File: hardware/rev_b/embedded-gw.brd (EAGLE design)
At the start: 38.5 x 55.5 mm, 57 parts, among them J1 DM3BT-DSF-PEJS, J2 TC2030-JLINK-NL, J3 USB-A-MALE-PLUG, Q1 DMN32D2LDF, U1 AP7362A-33SP-13, U2 BT840X, U3 CP2102N-20, U4 ESDR0502N, U5 ESP32-WROVER-E, U6 ESP32-WROVER-E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

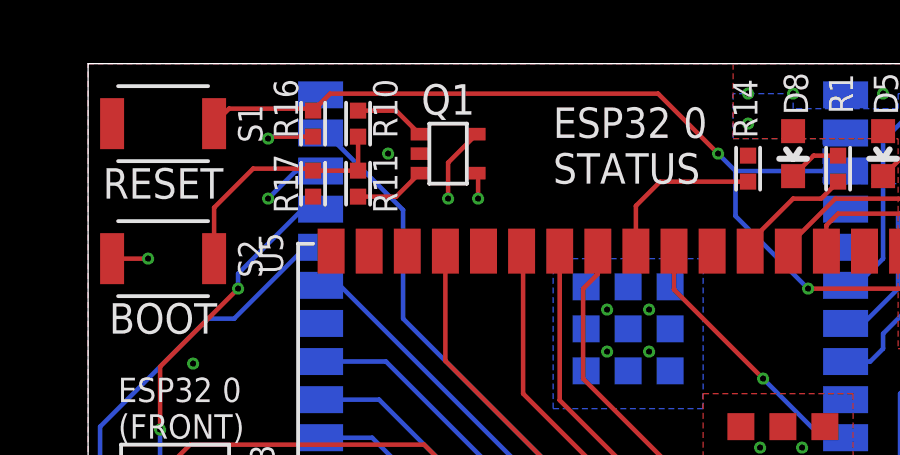
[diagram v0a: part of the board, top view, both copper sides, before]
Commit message: Swap Q1 with QS5K2TR
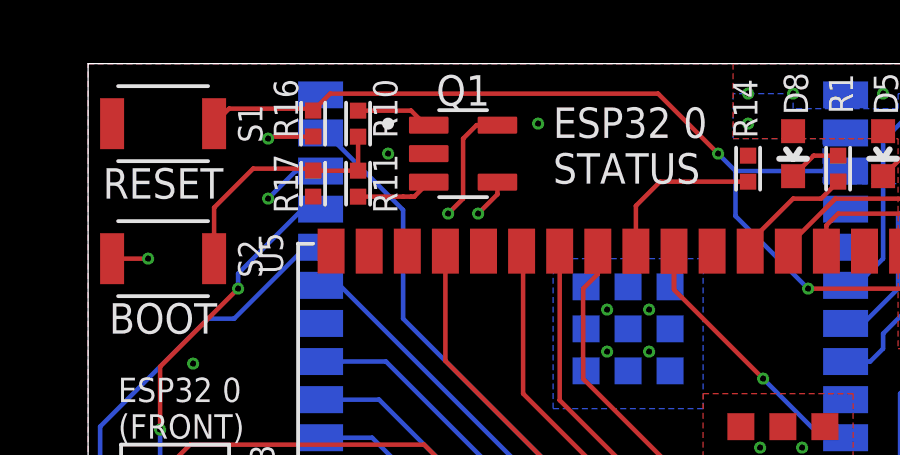
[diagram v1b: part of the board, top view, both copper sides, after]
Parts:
- Q1: value DMN32D2LDF -> QS5K2TR; device fets:SOT353 -> fets:SOT95P280X100-5N
- moved Q1 0.50 mm to (12.5, 52.5), turned to 0 degrees
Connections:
- net GND: now also Q1.2; no longer Q1.S
- net IO0: now also Q1.5; no longer Q1.D1
- net N$1: now also Q1.1; no longer Q1.G1
- net N$4: now also Q1.3; no longer Q1.G2
- net SD_HOST_D0: now also Q1.4; no longer Q1.D2
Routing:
- net IO0: track 27.6 -> 28.6 mm
- net GND: vias 43 -> 44
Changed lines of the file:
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@@
 <layer number="25" name="tNames" color="7" fill="1" visible="yes" active="yes"/>
 <layer number="26" name="bNames" color="7" fill="1" visible="yes" active="yes"/>
-<layer number="27" name="tValues" color="7" fill="1" visible="yes" active="yes"/>
+<layer number="27" name="tValues" color="7" fill="1" visible="no" active="yes"/>
 <layer number="28" name="bValues" color="7" fill="1" visible="no" active="yes"/>
 <layer number="29" name="tStop" color="7" fill="3" visible="no" active="yes"/>
@@
 <attribute name="VALUE" x="7.603" y="51.5" size="1.016" layer="27" font="vector" ratio="12" rot="R270" align="bottom-center"/>
 </element>
-<element name="Q1" library="fets" package="SOT353" value="DMN32D2LDF" x="12" y="52.5" smashed="yes" rot="R90">
-<attribute name="DIGIKEY" value="DMN32D2LDF-7DICT-ND" x="12" y="52.5" size="1.778" layer="27" rot="R90" display="off"/>
-<attribute name="MANUFACTURER" value="Diodes Incorporated" x="12" y="52.5" size="1.778" layer="27" rot="R90" display="off"/>
-<attribute name="MPN" value="DMN32D2LDF-7" x="12" y="52.5" size="1.778" layer="27" rot="R90" display="off"/>
-<attribute name="NAME" x="12" y="53.8" size="1.016" layer="25" font="vector" ratio="12" align="bottom-center"/>
-<attribute name="VALUE" x="12" y="54.2905" size="1.016" layer="27" font="vector" ratio="12" rot="R180" align="top-center"/>
+<element name="Q1" library="fets" package="SOT95P280X100-5N" value="QS5K2TR" x="12.5" y="52.5" smashed="yes">
+<attribute name="NAME" x="12.5" y="54.1" size="1.016" layer="25" font="vector" ratio="12" align="bottom-center"/>
+<attribute name="VALUE" x="14.2905" y="52.5" size="1.016" layer="27" font="vector" ratio="12" rot="R90" align="top-center"/>
 </element>
 <element name="D2" library="passives" package="0201_DIODE" value="" x="18" y="22" smashed="yes" rot="MR270">
@@
 <contactref element="S1" pad="1"/>
 <contactref element="R17" pad="1"/>
-<contactref element="Q1" pad="S"/>
+<contactref element="Q1" pad="2"/>
 <via x="10" y="52.5" extent="1-16" drill="0.2032"/>
 <contactref element="D2" pad="P$2"/>
@@
 <via x="3" y="30.5" extent="1-16" drill="0.2032"/>
 <via x="3.5" y="45.5" extent="1-16" drill="0.2032"/>
+<via x="15" y="53.5" extent="1-16" drill="0.2032"/>
 </signal>
 <signal name="VCC">
@@
 <wire x1="13.5" y1="21.5" x2="13" y2="22" width="0.1524" layer="2"/>
 <wire x1="13" y1="30" x2="13" y2="22" width="0.1524" layer="2"/>
-<contactref element="Q1" pad="D2"/>
-<via x="13" y="51" extent="1-16" drill="0.2032"/>
+<contactref element="Q1" pad="4"/>
+<via x="13" y="50.5" extent="1-16" drill="0.2032"/>
 <via x="13" y="38" extent="1-16" drill="0.2032"/>
-<wire x1="13" y1="51" x2="13" y2="38" width="0.1524" layer="2"/>
+<wire x1="13" y1="50.5" x2="13" y2="38" width="0.1524" layer="2"/>
 <wire x1="13" y1="33.5" x2="13" y2="38" width="0.1524" layer="1"/>
-<wire x1="12.95" y1="51.85" x2="13" y2="51.8" width="0.1524" layer="1"/>
-<wire x1="13" y1="51.8" x2="13" y2="51" width="0.1524" layer="1"/>
+<wire x1="13.645" y1="51.55" x2="13.645" y2="51.145" width="0.1524" layer="1"/>
+<wire x1="13.645" y1="51.145" x2="13" y2="50.5" width="0.1524" layer="1"/>
 </signal>
 <signal name="SD_HOST_D1">
@@
 <signal name="N$1">
 <contactref element="R10" pad="2"/>
-<contactref element="Q1" pad="G1"/>
-<wire x1="9" y1="53.93306875" x2="10.26693125" y2="53.93306875" width="0.1524" layer="1"/>
-<wire x1="10.26693125" y1="53.93306875" x2="11.05" y2="53.15" width="0.1524" layer="1"/>
+<contactref element="Q1" pad="1"/>
+<wire x1="10.76693125" y1="53.93306875" x2="9" y2="53.93306875" width="0.1524" layer="1"/>
+<wire x1="11.355" y1="53.45" x2="11.25" y2="53.45" width="0.1524" layer="1"/>
+<wire x1="11.25" y1="53.45" x2="10.76693125" y2="53.93306875" width="0.1524" layer="1"/>
 </signal>
 <signal name="N$4">
-<contactref element="Q1" pad="G2"/>
+<contactref element="Q1" pad="3"/>
 <contactref element="R11" pad="2"/>
-<wire x1="9" y1="51.06693125" x2="10.26693125" y2="51.06693125" width="0.1524" layer="1"/>
-<wire x1="10.26693125" y1="51.06693125" x2="11.05" y2="51.85" width="0.1524" layer="1"/>
+<wire x1="9" y1="51.06693125" x2="10.5" y2="51.06693125" width="0.1524" layer="1"/>
+<wire x1="10.5" y1="51.06693125" x2="10.76693125" y2="51.06693125" width="0.1524" layer="1"/>
+<wire x1="10.76693125" y1="51.06693125" x2="10.87193125" y2="51.06693125" width="0.1524" layer="1"/>
+<wire x1="10.87193125" y1="51.06693125" x2="11.355" y2="51.55" width="0.1524" layer="1"/>
 </signal>
 <signal name="IO0">
-<contactref element="Q1" pad="D1"/>
+<contactref element="Q1" pad="5"/>
 <contactref element="U5" pad="25"/>
 <contactref element="U6" pad="25"/>
 <via x="14.5" y="33.5" extent="1-16" drill="0.2032"/>
-<via x="12" y="51" extent="1-16" drill="0.2032"/>
-<wire x1="12" y1="51" x2="12" y2="37" width="0.1524" layer="2"/>
+<via x="12" y="50.5" extent="1-16" drill="0.2032"/>
+<wire x1="12" y1="50.5" x2="12" y2="37" width="0.1524" layer="2"/>
 <wire x1="12" y1="37" x2="11.5" y2="36.5" width="0.1524" layer="2"/>
 <wire x1="7.75" y1="37.95" x2="10.05" y2="37.95" width="0.1524" layer="16"/>
@@
 <wire x1="14.45" y1="33.45" x2="14.5" y2="33.5" width="0.1524" layer="1"/>
 <via x="11.5" y="36.5" extent="1-16" drill="0.2032"/>
-<wire x1="12.95" y1="53.15" x2="12" y2="52.2" width="0.1524" layer="1"/>
-<wire x1="12" y1="52.2" x2="12" y2="51" width="0.1524" layer="1"/>
+<wire x1="13.645" y1="53.45" x2="12.95" y2="53.45" width="0.1524" layer="1"/>
+<wire x1="12.95" y1="53.45" x2="12.5" y2="53" width="0.1524" layer="1"/>
+<wire x1="12.5" y1="51" x2="12" y2="50.5" width="0.1524" layer="1"/>
+<wire x1="12.5" y1="53" x2="12.5" y2="51" width="0.1524" layer="1"/>
 </signal>
 <signal name="N$10">
